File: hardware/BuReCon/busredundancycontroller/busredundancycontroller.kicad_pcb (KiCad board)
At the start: 2 copper layers, 2 x 7.5 mm, 87 parts, among them J1 USB_B_Micro, J2 Clock Output, J3 Differential IO, J4 Input/Output 1, J5 Input/Output 2, J6 Input/Output 3, J7 Input/Output 4, J8 Input/Output 5, U1 ICE40LP1K-CM36, U2 AP7361C-33E, U3 AP7361C-12E, U4 USBLC6-2SC6, U5 FT2232HL, U6 93LC56C, U7 DSC1001DI1, U8 SST26VF032B

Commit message: PCB preliminary placement
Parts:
- moved FB3 133.8 mm to (104.8, 90.2)
- moved LD1 133.8 mm to (123.5, 94.5)
- moved FB2 131.4 mm to (106.5, 87.2)
- moved C18 130.5 mm to (102.0, 85.8), turned to 180 degrees
- moved C10 129.5 mm to (119.0, 96.8), turned to 90 degrees
- moved R13 128.7 mm to (121.0, 80.0)
- moved C9 127.1 mm to (117.2, 96.8), turned to 90 degrees
- moved R9 127.0 mm to (116.0, 78.5)
- moved C16 126.4 mm to (106.5, 85.8)
- moved R10 126.3 mm to (116.0, 80.0)
- moved C11 126.1 mm to (104.0, 96.2), turned to 90 degrees
- moved R3 124.8 mm to (108.8, 85.0), turned to 270 degrees
- moved C17 124.6 mm to (106.5, 84.2)
- moved C19 124.4 mm to (102.0, 84.2), turned to 180 degrees
- moved R2 124.2 mm to (105.8, 88.8)
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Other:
- board size 2 x 7.5 mm -> 50 x 50 mm

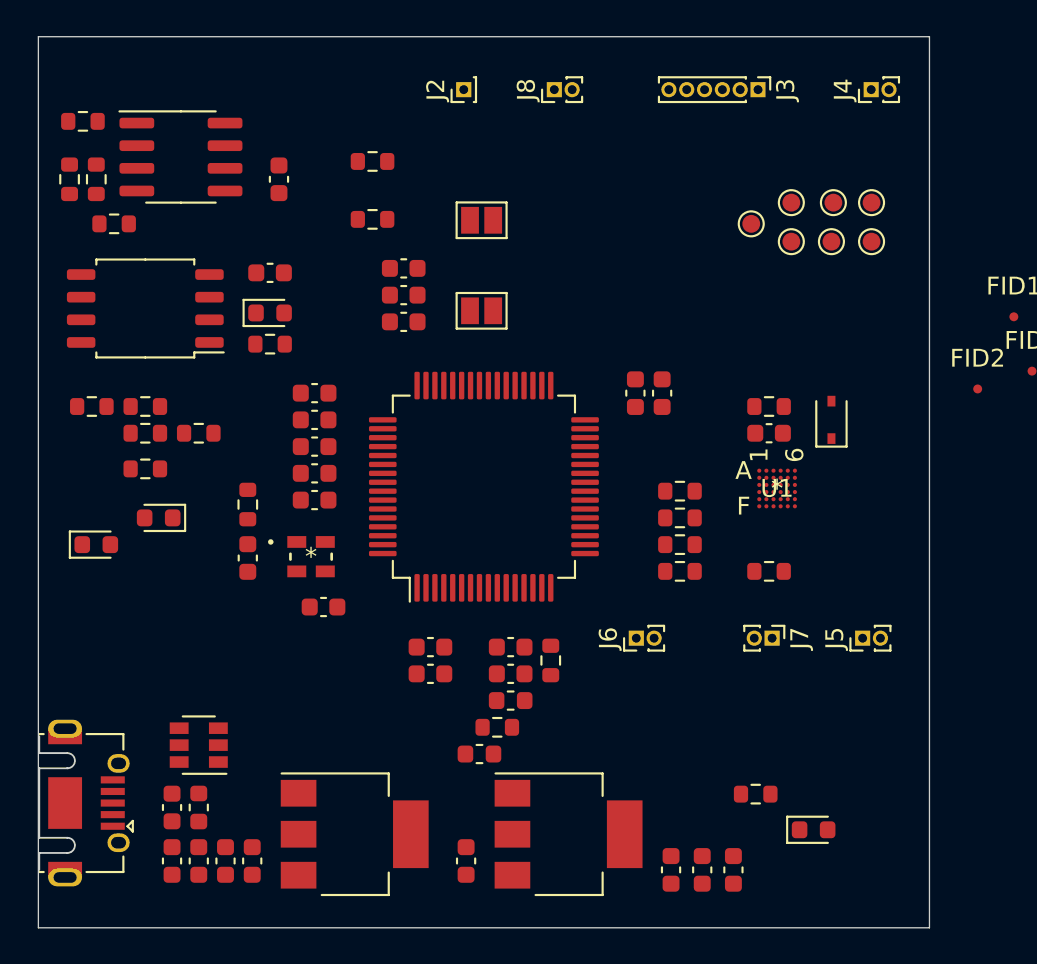
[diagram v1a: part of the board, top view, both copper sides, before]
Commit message: PBC placement. Silk
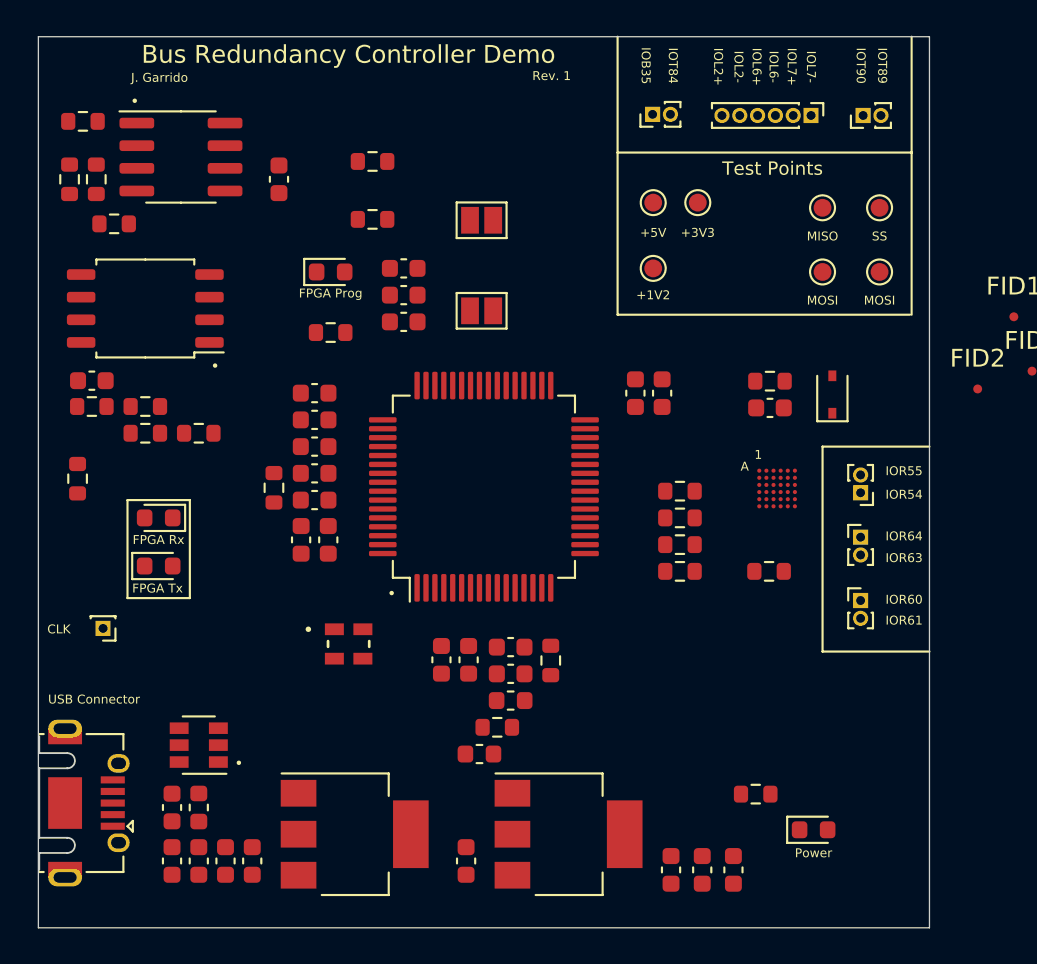
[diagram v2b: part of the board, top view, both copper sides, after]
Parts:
- moved J2 36.4 mm to (83.6, 83.2), turned to 180 degrees
- moved J6 12.8 mm to (126.1, 81.6), turned to 0 degrees
- moved TP1 12.2 mm to (114.5, 59.3)
- moved C28 11.7 mm to (83.0, 69.3)
- moved TP3 10.8 mm to (114.5, 63.0)
- moved J5 8.16 mm to (126.1, 75.6), turned to 180 degrees
- moved J7 7.54 mm to (126.1, 78.1), turned to 0 degrees
- moved J8 5.69 mm to (114.5, 54.4)
- moved U7 5.33 mm to (97.4, 84.1)
- moved TP2 5.25 mm to (117.0, 59.3)
- moved TP5 4.83 mm to (124.0, 63.2)
- moved LD2 4.10 mm to (96.4, 63.2)
- moved R19 3.84 mm to (82.2, 74.8), turned to 90 degrees
- moved C25 3.78 mm to (96.3, 78.2), turned to 90 degrees
- moved LD3 3.70 mm to (86.8, 79.7)
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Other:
- board text added: "+1V2"
- board text added: "+3V3"
- board text added: "+5V"
- board text added: "1"
- board text added: "Bus Redundancy Controller Demo"
- board text added: "CLK"
- board text added: "FPGA Prog"
- board text added: "FPGA Rx"
- board text added: "FPGA Tx"
- board text added: "IOB35"
- board text added: "IOL2+"
- board text added: "IOL2-"
- board text added: "IOL6+"
- board text added: "IOL6-"
- board text added: "IOL7+"
- board text added: "IOL7-"
- board text added: "IOR54"
- board text added: "IOR55"
- board text added: "IOR60"
- board text added: "IOR61"
- board text added: "IOR63"
- board text added: "IOR64"
- board text added: "IOT84"
- board text added: "IOT89"
- board text added: "IOT90"
- board text added: "J. Garrido"
- board text added: "MISO"
- board text added: "MOSI"
- board text added: "Power"
- board text added: "Rev. 1"
- board text added: "SS"
- board text added: "Test Points"
- board text added: "USB Connector"

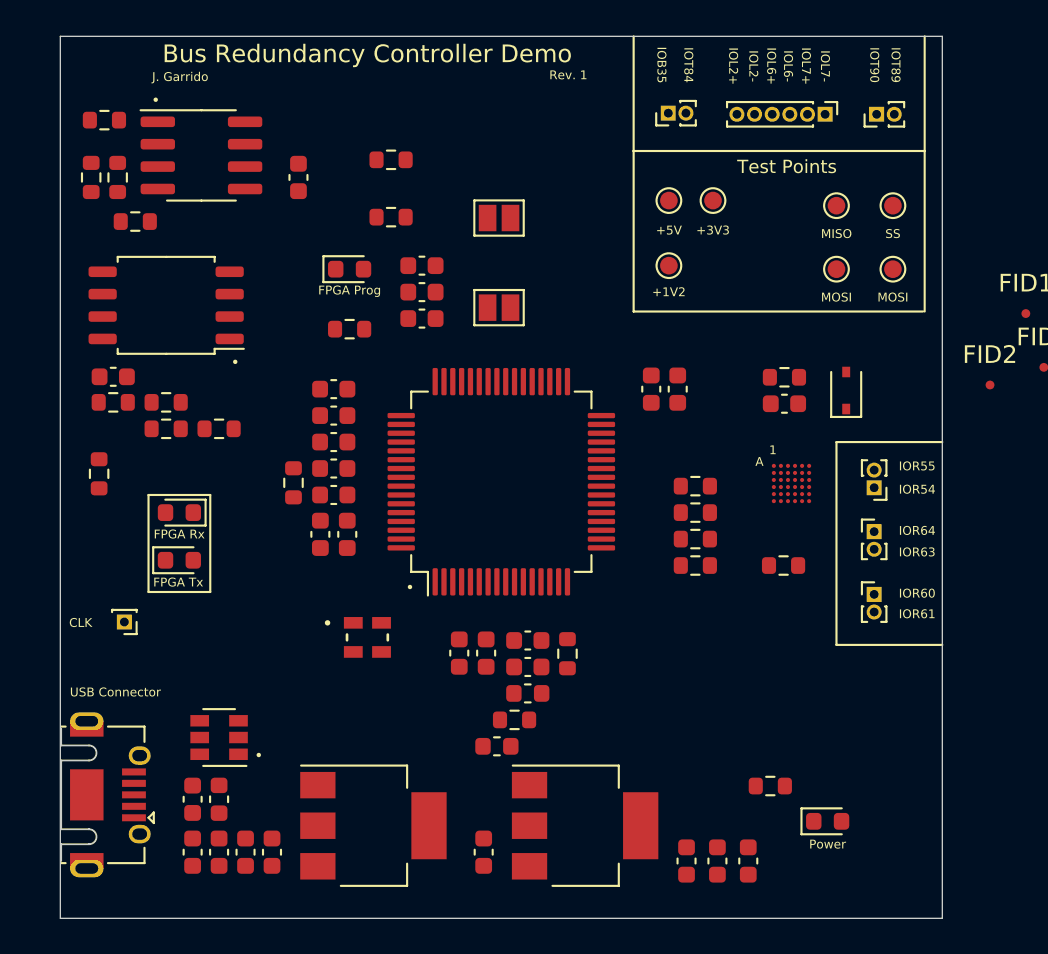
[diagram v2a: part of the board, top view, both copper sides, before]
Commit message: Fixed some DRC errors. Added pour zones
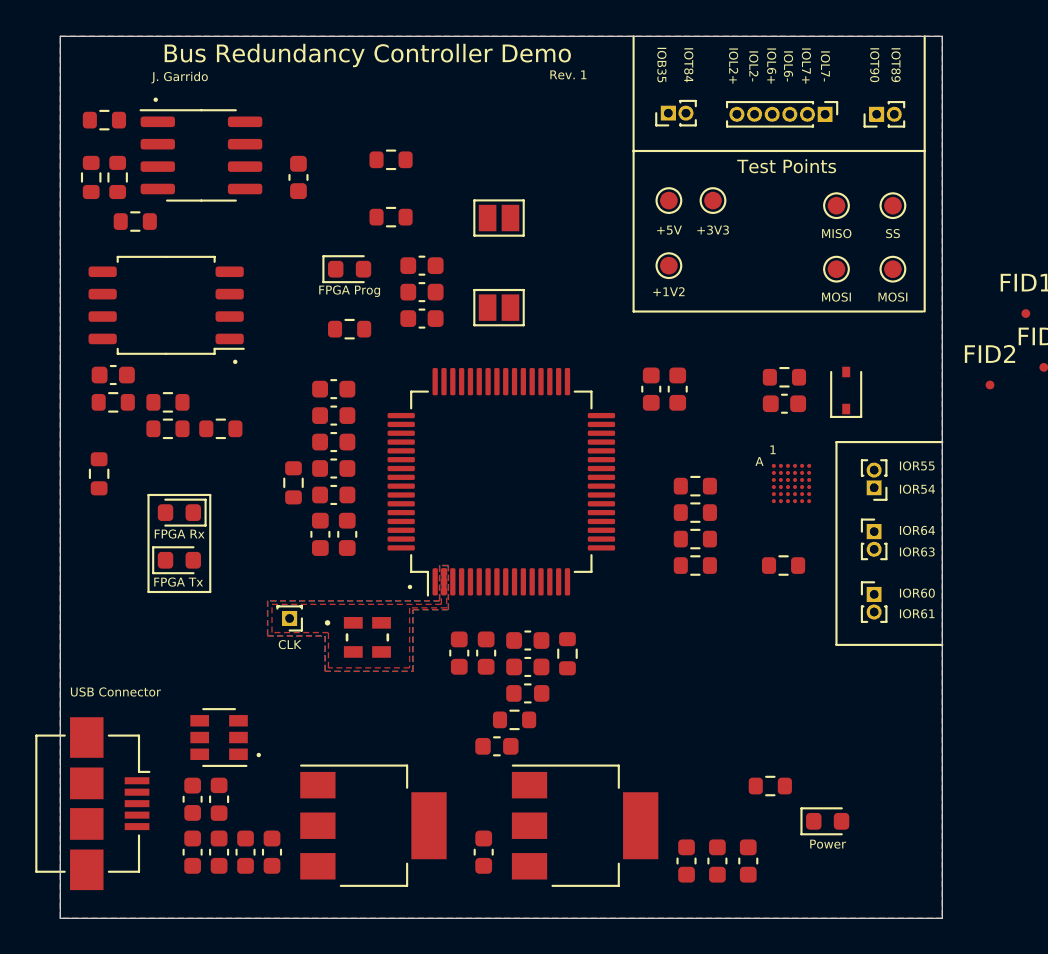
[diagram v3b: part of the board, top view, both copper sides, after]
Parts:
- J1: footprint Connector_USB:USB_Micro-AB_Molex_47590-0001 -> Connector_USB:USB_Micro-B_Amphenol_10104110_Horizontal
- moved J2 9.37 mm to (93.0, 83.0)
- moved J1 1.39 mm to (82.8, 93.5)
- moved C28 0.10 mm to (83.0, 69.2)
- moved R14 0.10 mm to (86.1, 70.8)
- moved R15 0.10 mm to (86.1, 72.2)
- moved R17 0.10 mm to (89.1, 72.2)
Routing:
- added copper zone on B.Cu, net GND
- added copper zone on F.Cu, net GND
- added copper zone on In1.Cu, net GND
- added copper zone on In2.Cu, net VCCIO_0_1
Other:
- copper layers 2 -> 4

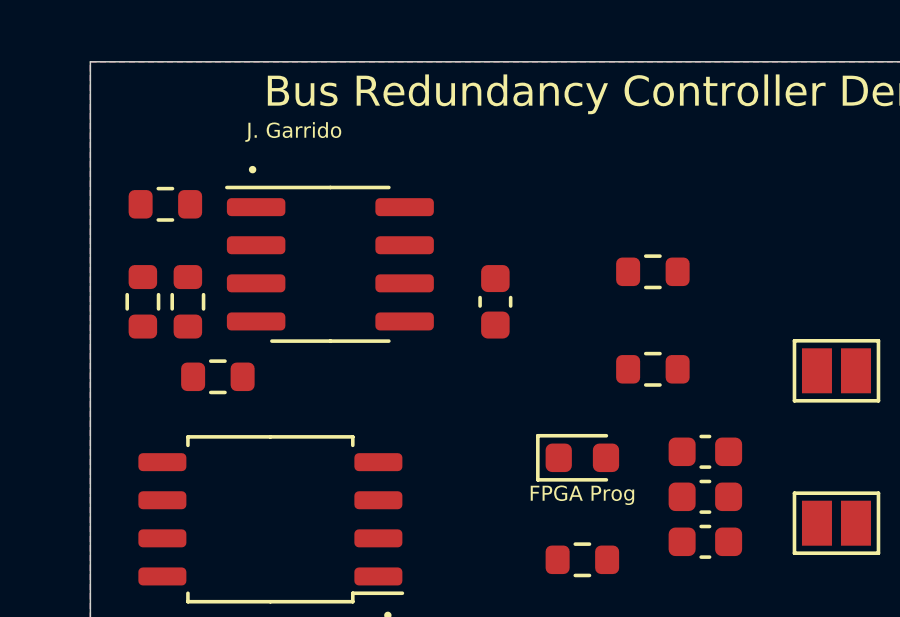
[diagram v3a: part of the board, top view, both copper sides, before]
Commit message: Correct nets in every layer
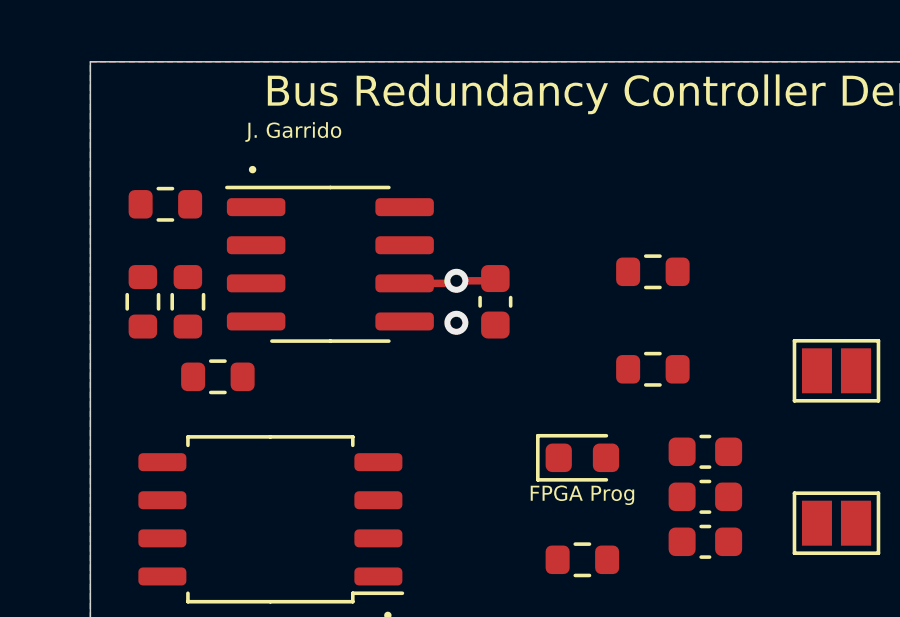
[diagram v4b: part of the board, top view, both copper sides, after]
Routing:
- net VCCIO_0_1: track 0.00 -> 3.09 mm, vias 0 -> 1
- net GND: vias 0 -> 1
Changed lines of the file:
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@@
     (thickness 1.6)
     (drawings 55)
-    (tracks 0)
+    (tracks 6)
     (zones 0)
     (modules 87)
@@
     (37 F.SilkS user)
     (38 B.Mask user)
-    (39 F.Mask user hide)
+    (39 F.Mask user)
     (40 Dwgs.User user)
     (41 Cmts.User user)
@@
   (gr_line (start 130 50) (end 130 100) (layer Edge.Cuts) (width 0.05))
   (gr_line (start 80 50) (end 130 50) (layer Edge.Cuts) (width 0.05))
+  (via (at 92.2 58.7) (size 0.8) (drill 0.4) (layers F.Cu B.Cu) (net 2))
+  (via (at 92.2 57.3) (size 0.8) (drill 0.4) (layers F.Cu B.Cu) (net 4))
+  (segment (start 92.115 57.385) (end 92.2 57.3) (width 0.25) (layer F.Cu) (net 4))
+  (segment (start 90.475 57.385) (end 92.115 57.385) (width 0.25) (layer F.Cu) (net 4))
+  (segment (start 93.425 57.3) (end 93.5 57.225) (width 0.25) (layer F.Cu) (net 4))
+  (segment (start 92.2 57.3) (end 93.425 57.3) (width 0.25) (layer F.Cu) (net 4))
   (zone (net 4) (net_name VCCIO_0_1) (layer In2.Cu) (hatch edge 0.508)
     (connect_pads (clearance 0.508))

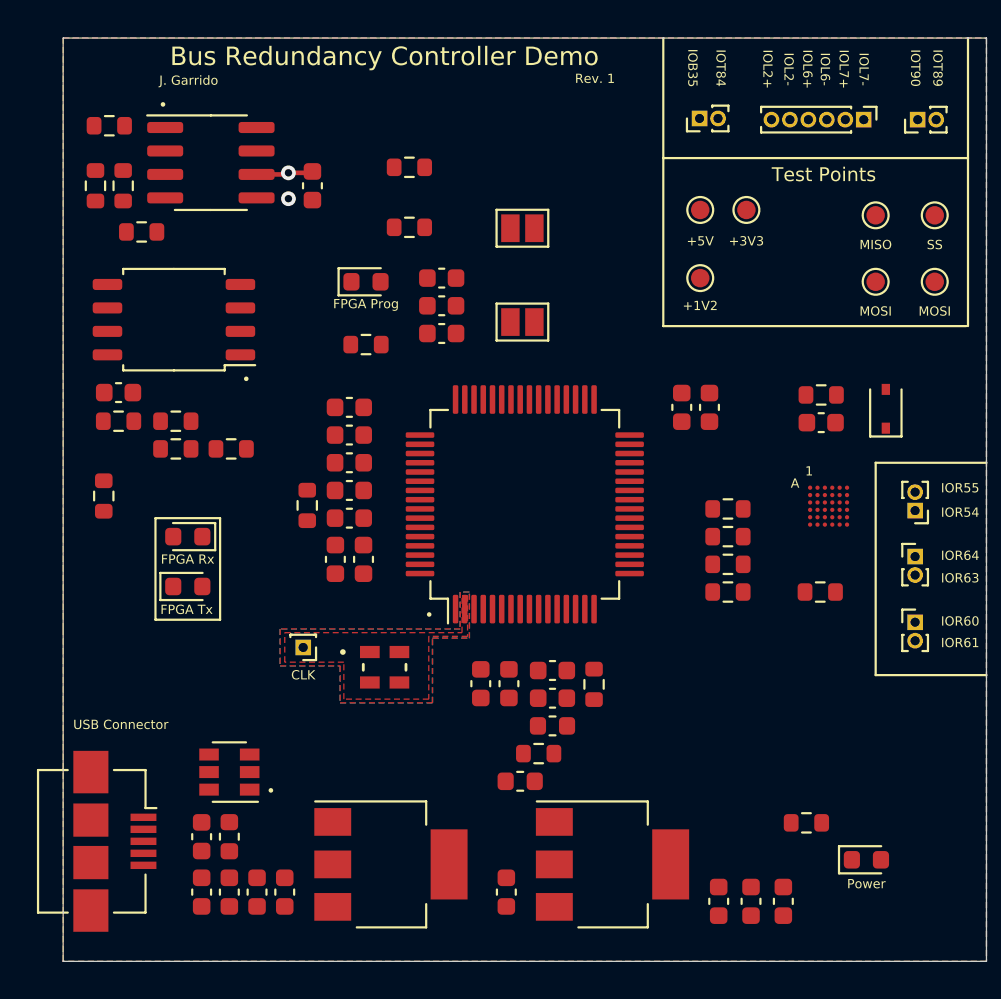
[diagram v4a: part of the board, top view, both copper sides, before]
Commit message: Routing power
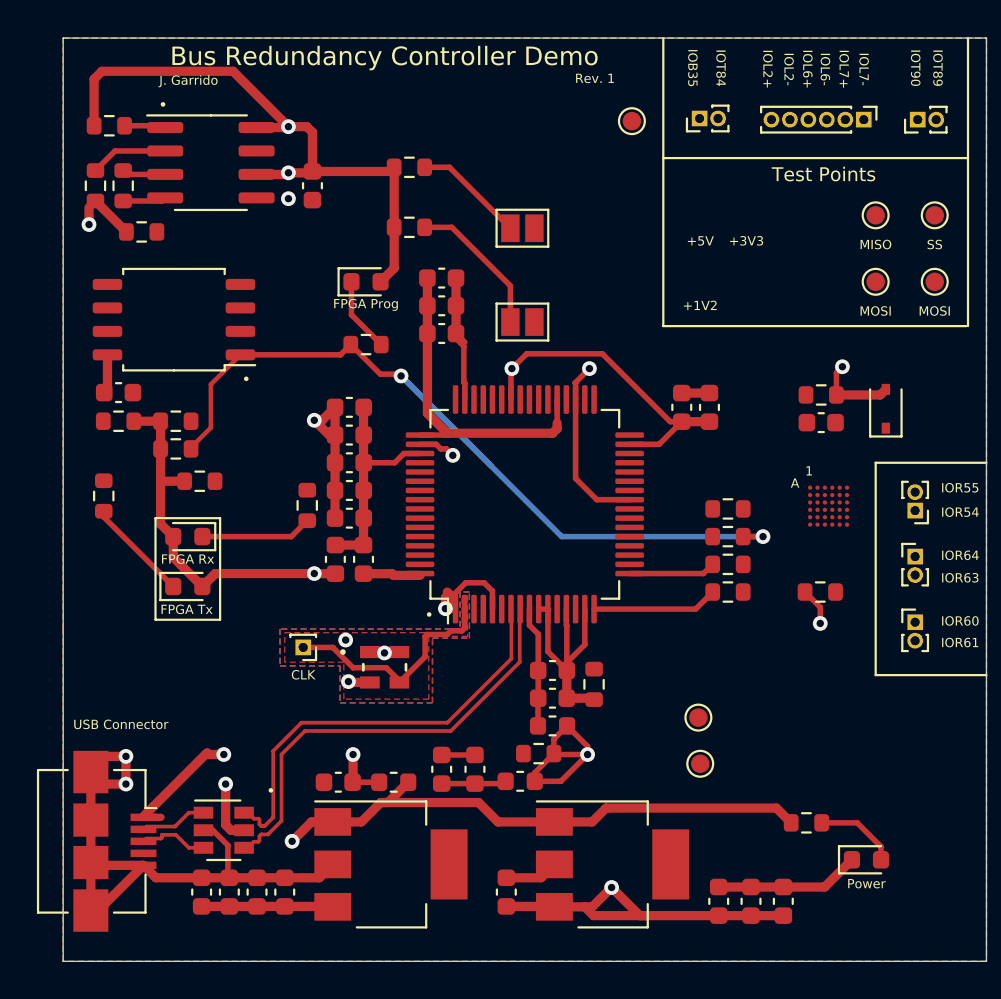
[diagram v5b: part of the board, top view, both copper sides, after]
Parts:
- moved TP1 30.0 mm to (114.5, 89.3)
- moved TP3 23.8 mm to (114.4, 86.8)
- moved FB1 9.38 mm to (97.9, 90.3), turned to 180 degrees
- moved C1 7.97 mm to (94.9, 90.3), turned to 180 degrees
- moved TP2 7.85 mm to (110.8, 54.5)
- moved C18 5.10 mm to (100.5, 89.6), turned to 90 degrees
- moved C19 4.99 mm to (102.3, 89.6), turned to 90 degrees
- moved U4 3.16 mm to (88.7, 92.9), turned to 0 degrees
- moved R17 2.44 mm to (87.4, 74.0)
- turned R18 to 0 degrees
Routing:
- net VCCIO_0_1: track 3.09 -> 129.8 mm, vias 1 -> 12
- net GND: track 0.00 -> 103.0 mm, vias 1 -> 7
- net F_SS: track 0.00 -> 47.1 mm, vias 0 -> 2
- net +5V: track 0.00 -> 40.5 mm, vias 0 -> 2
- net USB_D+: track 0.00 -> 24.2 mm
- net USB_D-: track 0.00 -> 23.5 mm
- net +1V8: track 0.00 -> 21.1 mm
- net Net-(C1-Pad1): track 0.00 -> 16.6 mm, vias 0 -> 2
- net GCLOCK: track 0.00 -> 12.5 mm
- net Net-(JP1-Pad1): track 0.00 -> 7.92 mm
- net +1V2: track 0.00 -> 7.11 mm
- net FPGA_SCK: track 0.00 -> 6.81 mm
- net Net-(C16-Pad1): track 0.00 -> 6.53 mm
- net Net-(LD4-Pad1): track 0.00 -> 6.04 mm
- net Net-(JP2-Pad1): track 0.00 -> 6.01 mm
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
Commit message: last minute changes
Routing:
- net F_MOSI: track 0.00 -> 60.0 mm, vias 0 -> 8
- net F_CLK: track 0.00 -> 55.3 mm, vias 0 -> 4
- net FT_CS: track 2.24 -> 41.1 mm, vias 0 -> 4
- net FT_DATA: track 2.36 -> 38.7 mm, vias 0 -> 4
- net FT_SCLK: track 4.21 -> 40.5 mm, vias 0 -> 4
- net F_MISO: track 0.00 -> 35.4 mm, vias 0 -> 6
- net GCLOCK: track 12.5 -> 31.1 mm, vias 0 -> 2
- net Net-(R19-Pad2): track 0.00 -> 18.2 mm, vias 0 -> 4
- net FT_RXD: track 0.00 -> 17.2 mm, vias 0 -> 2
- net FT_TXD: track 0.00 -> 14.2 mm, vias 0 -> 2
- net Net-(R22-Pad2): track 0.00 -> 12.5 mm, vias 0 -> 2
- net FPGA_CREST: track 0.00 -> 12.1 mm, vias 0 -> 2
- net Net-(R17-Pad2): track 0.00 -> 11.3 mm, vias 0 -> 2
- net Net-(C18-Pad1): track 3.54 -> 14.6 mm, vias 0 -> 2
- net Net-(R3-Pad1): track 0.00 -> 10.8 mm, vias 0 -> 2
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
